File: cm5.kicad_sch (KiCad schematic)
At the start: 14 parts, among them J2 CM5_1-100_3mm-stack, J3 CM5_101-200_3mm-stack, J4 JST_SH_1x3_BM03B-SRSS-TB-LF-SN

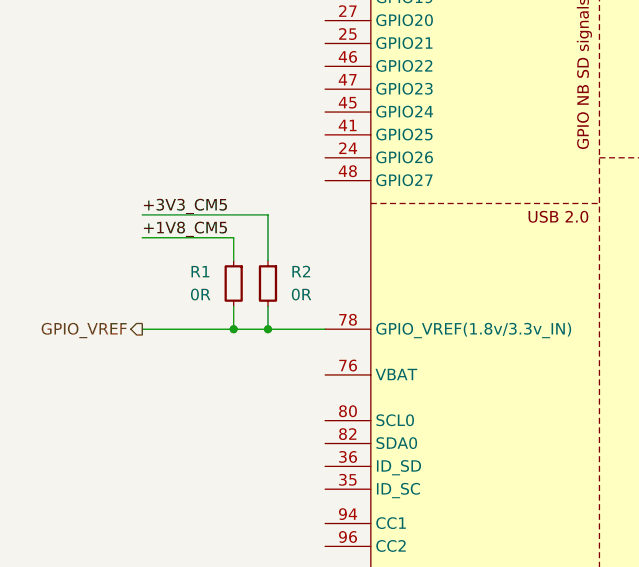
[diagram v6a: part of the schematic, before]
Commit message: [#1] Add power section
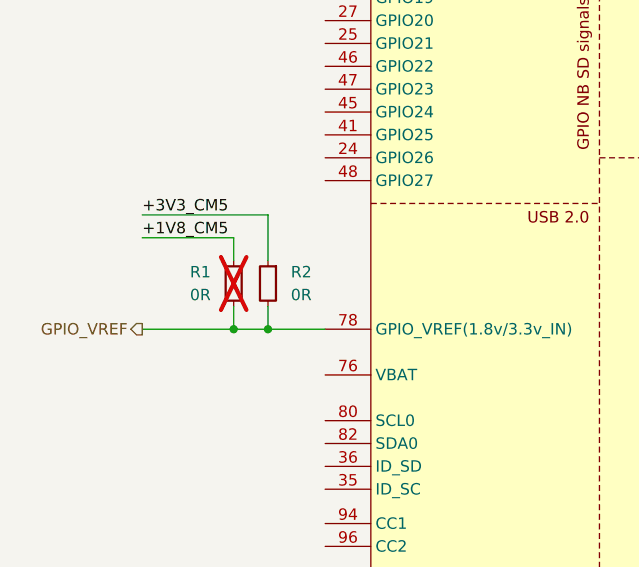
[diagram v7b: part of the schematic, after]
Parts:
- R1: now not fitted
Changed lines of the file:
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@@
 		(polyline
 			(pts
-				(xy 171.45 85.09) (xy 171.45 115.57) (xy 149.86 115.57) (xy 149.86 85.09)
+				(xy 243.84 162.56) (xy 217.17 162.56) (xy 217.17 119.38) (xy 243.84 119.38)
 			)
 			(stroke
@@
 		(polyline
 			(pts
-				(xy 243.84 162.56) (xy 217.17 162.56) (xy 217.17 119.38) (xy 243.84 119.38)
+				(xy 243.84 114.3) (xy 217.17 114.3) (xy 217.17 96.52) (xy 243.84 96.52)
 			)
 			(stroke
@@
 		(polyline
 			(pts
-				(xy 243.84 114.3) (xy 217.17 114.3) (xy 217.17 96.52) (xy 243.84 96.52)
+				(xy 171.45 85.09) (xy 171.45 115.57) (xy 149.86 115.57) (xy 149.86 85.09)
 			)
 			(stroke
@@
 		(in_bom yes)
 		(on_board yes)
-		(dnp no)
+		(dnp yes)
 		(fields_autoplaced yes)
 		(property "Reference" "R1"
